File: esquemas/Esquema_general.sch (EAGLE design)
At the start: 36 parts

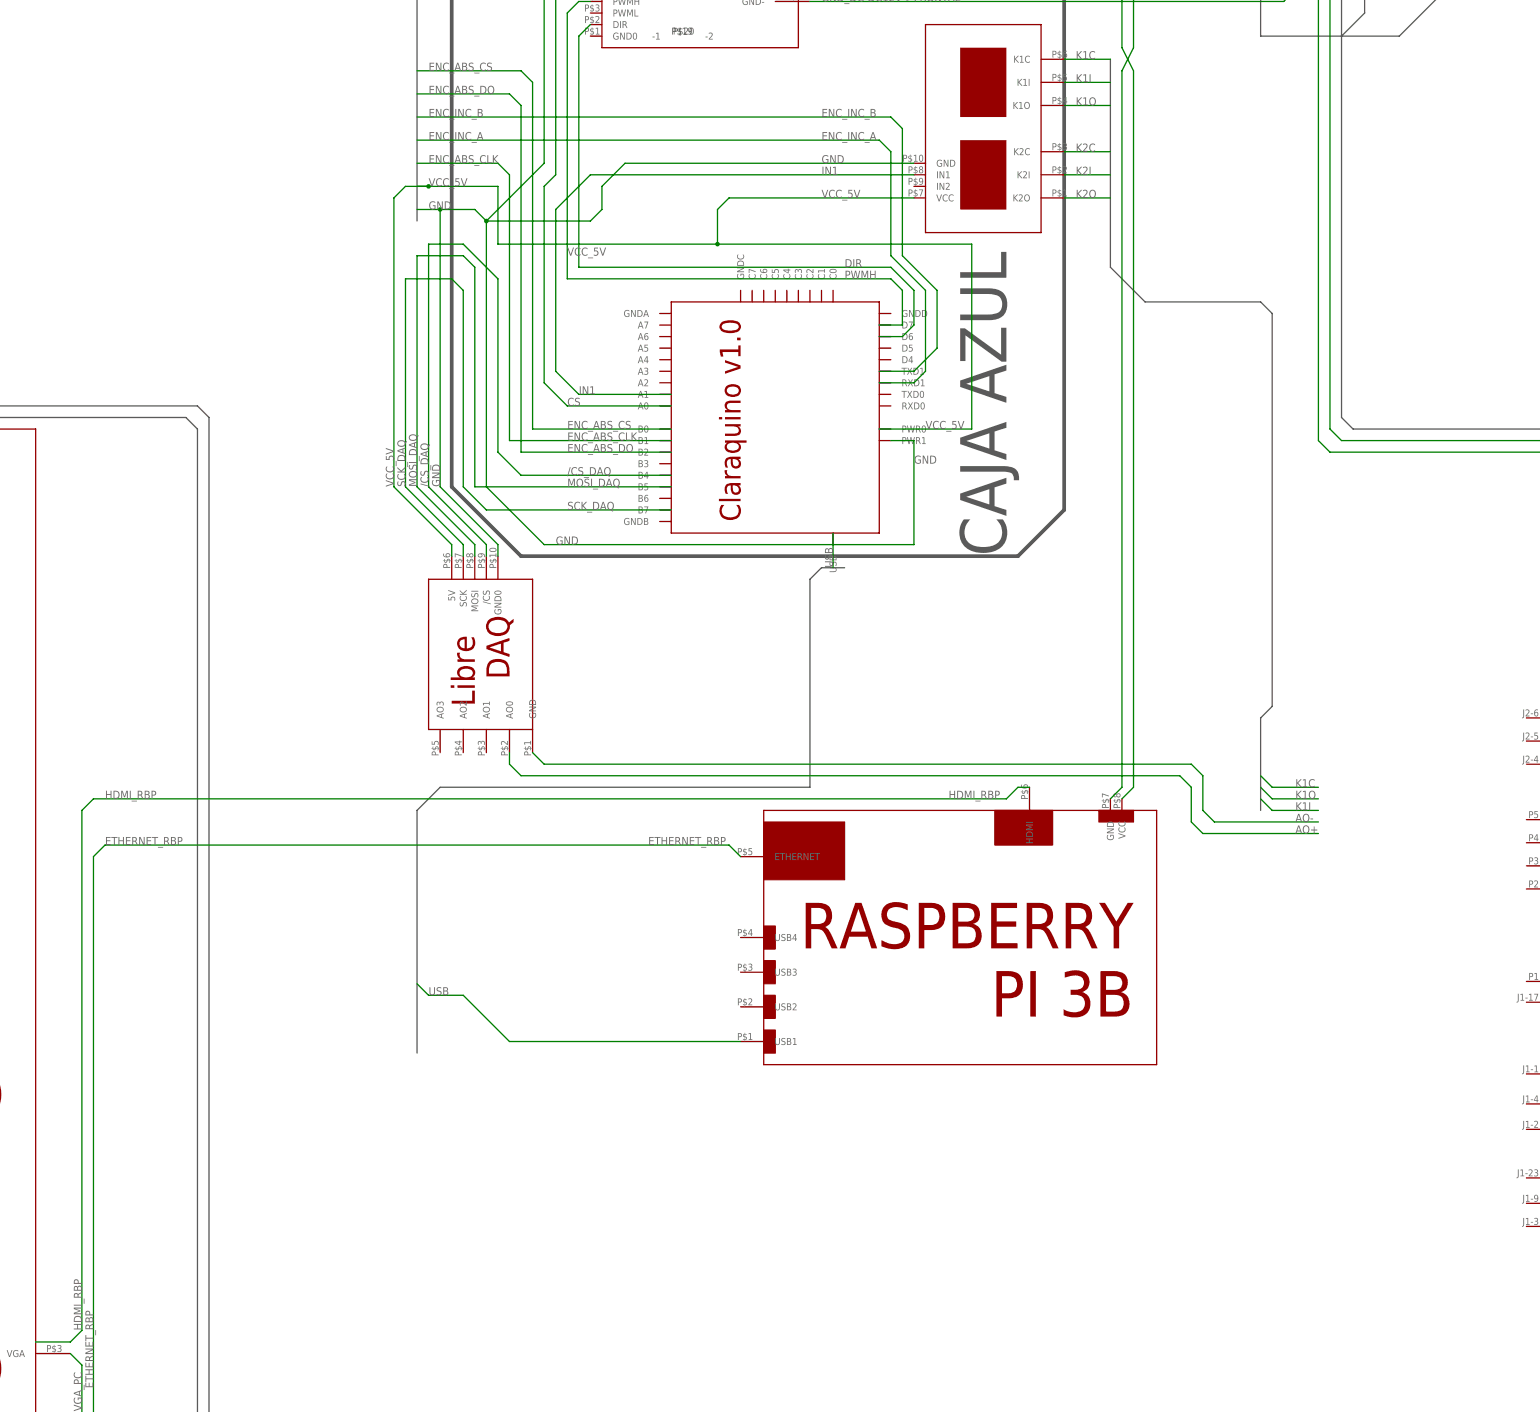
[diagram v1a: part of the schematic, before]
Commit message: sch eagle: quitar RBPI, añadir cables segundo rele
TODO: Curtis sch
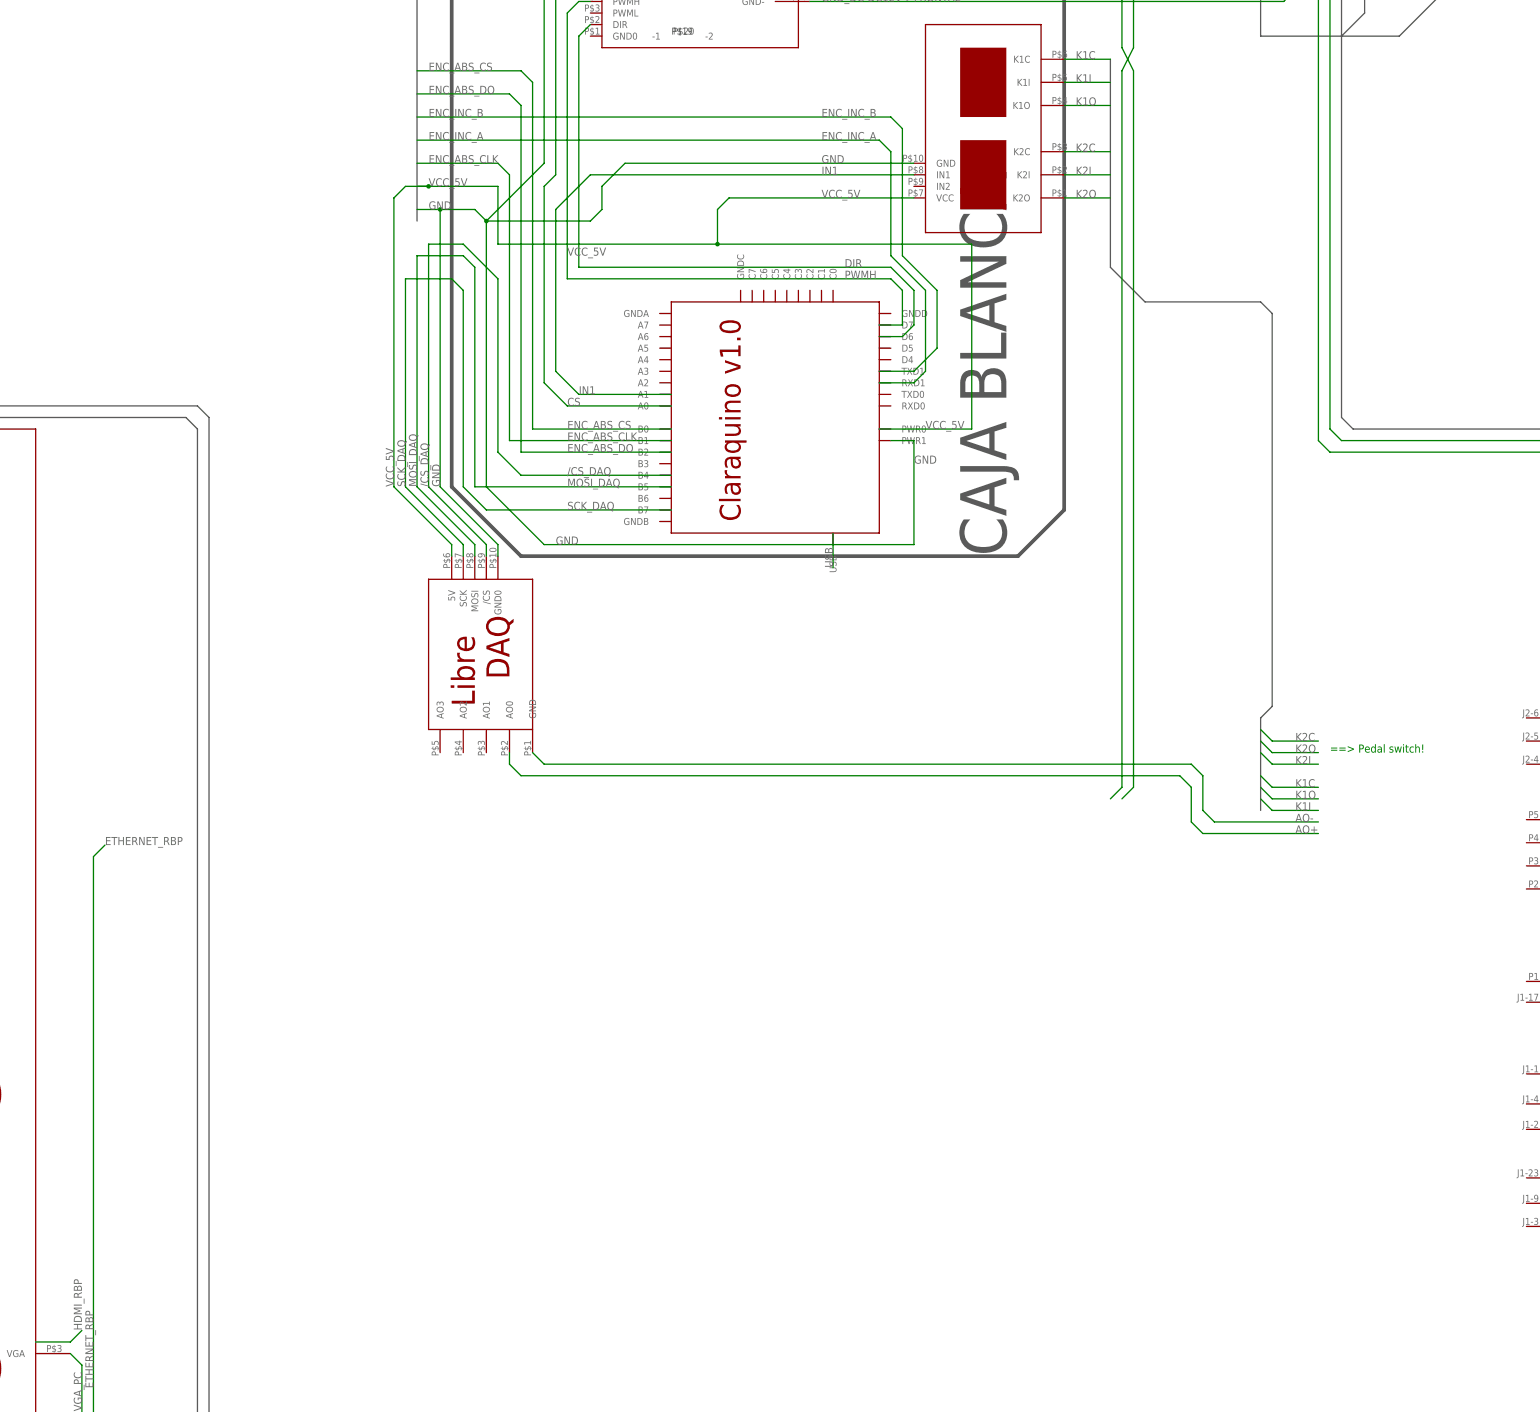
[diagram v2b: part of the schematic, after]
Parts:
- removed U$31: RASPBERRY_PI_3B, ecar:RASPBERRY_PI_3B
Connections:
- removed net ETHERNET_RBP: U$31.ETHERNET
- removed net HDMI_RBP: U$31.HDMI
- net 5V_GND: no longer U$31.GND
- net 5V_VCC: no longer U$31.VCC
- net USB: no longer U$31.USB1
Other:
- note added: "==> Pedal switch!"
- note removed: "CAJA AZUL"
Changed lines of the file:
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@@
 <?xml version="1.0" encoding="utf-8"?>
 <!DOCTYPE eagle SYSTEM "eagle.dtd">
-<eagle version="8.5.0">
+<eagle version="7.5.0">
 <drawing>
 <settings>
@@
 <part name="U$29" library="ecar" deviceset="SICK" device=""/>
 <part name="U$30" library="ecar" deviceset="MOTOR_SENSORES" device=""/>
-<part name="U$31" library="ecar" deviceset="RASPBERRY_PI_3B" device=""/>
 <part name="U$1" library="ecar" deviceset="MOTOR_DIRECCION" device=""/>
 <part name="U$34" library="ecar" deviceset="POLOLU_HIGH-POWER_MOTOR_DRIVER" device=""/>
 <part name="U$35" library="ecar" deviceset="AMPERIMETRO" device=""/>
 <part name="U$17" library="ecar" deviceset="GPS" device=""/>
-<part name="D1" library="display-hp" library_urn="urn:adsk.eagle:library:212" deviceset="HLMP6" device="" package3d_urn="urn:adsk.eagle:package:12992/1"/>
+<part name="D1" library="display-hp" deviceset="HLMP6" device=""/>
 <part name="U$32" library="ecar" deviceset="RELE_ARDUINO" device=""/>
 <part name="U$36" library="ecar" deviceset="LIBRE_DAQ" device=""/>
@@
 <wire x1="1356.36" y1="467.36" x2="1356.36" y2="193.04" width="0.508" layer="90"/>
 <wire x1="1356.36" y1="193.04" x2="1353.82" y2="190.5" width="0.508" layer="90"/>
-<wire x1="1353.82" y1="190.5" x2="1155.7" y2="190.5" width="0.508" layer="90"/>
 <wire x1="1155.7" y1="190.5" x2="1153.16" y2="193.04" width="0.508" layer="90"/>
 <wire x1="1153.16" y1="193.04" x2="1153.16" y2="467.36" width="0.508" layer="90"/>
@@
 <text x="1391.92" y="444.5" size="1.778" layer="97" rot="R90">Manguera_Encoder_Absoluto</text>
 <text x="1584.96" y="472.44" size="1.778" layer="97">Manguera_Encoder_Absoluto</text>
-<text x="1295.4" y="307.34" size="10.16" layer="97" rot="R90">CAJA AZUL</text>
+<text x="1295.4" y="307.34" size="10.16" layer="97" rot="R90">CAJA BLANCA</text>
 <text x="1348.74" y="269.24" size="17.78" layer="90" rot="R90">CAJA BLANCA</text>
+<text x="1366.52" y="264.16" size="1.778" layer="91">==&gt; Pedal switch!</text>
+<wire x1="1155.7" y1="190.5" x2="1353.82" y2="190.5" width="0.508" layer="90"/>
 </plain>
 <instances>
@@
 <instance part="U$29" gate="G$1" x="1770.38" y="342.9" rot="R270"/>
 <instance part="U$30" gate="G$1" x="1676.4" y="-45.72" rot="R90"/>
-<instance part="U$31" gate="G$1" x="1328.42" y="251.46" rot="R180"/>
 <instance part="U$1" gate="G$1" x="1617.98" y="490.22" rot="R90"/>
 <instance part="U$34" gate="G$1" x="1206.5" y="419.1"/>
@@
 <label x="1254.76" y="487.68" size="1.778" layer="95"/>
 <label x="1369.06" y="444.5" size="1.778" layer="95" rot="R90"/>
-</segment>
-</bus>
-<bus name="B$1">
-<segment>
-<wire x1="1165.86" y1="198.12" x2="1165.86" y2="251.46" width="0.762" layer="92"/>
-<wire x1="1165.86" y1="251.46" x2="1170.94" y2="256.54" width="0.762" layer="92"/>
-<wire x1="1170.94" y1="256.54" x2="1252.22" y2="256.54" width="0.762" layer="92"/>
-<wire x1="1252.22" y1="256.54" x2="1252.22" y2="302.26" width="0.762" layer="92"/>
-<wire x1="1252.22" y1="302.26" x2="1254.76" y2="304.8" width="0.762" layer="92"/>
-<wire x1="1254.76" y1="304.8" x2="1259.84" y2="304.8" width="0.762" layer="92"/>
 </segment>
 </bus>
@@
 <wire x1="1069.34" y1="474.98" x2="1323.34" y2="474.98" width="0.508" layer="91"/>
 <wire x1="1323.34" y1="474.98" x2="1323.34" y2="419.1" width="0.508" layer="91"/>
-<pinref part="U$31" gate="G$1" pin="GND"/>
 <wire x1="1318.26" y1="254" x2="1320.8" y2="256.54" width="0.508" layer="91"/>
 <wire x1="1320.8" y1="256.54" x2="1320.8" y2="414.02" width="0.508" layer="91"/>
@@
 <wire x1="1320.8" y1="419.1" x2="1323.34" y2="414.02" width="0.508" layer="91"/>
 <wire x1="1323.34" y1="414.02" x2="1323.34" y2="256.54" width="0.508" layer="91"/>
-<pinref part="U$31" gate="G$1" pin="VCC"/>
 <wire x1="1323.34" y1="256.54" x2="1320.8" y2="254" width="0.508" layer="91"/>
 <label x="1254.76" y="472.44" size="1.778" layer="95"/>
@@
 <label x="1310.64" y="386.08" size="1.778" layer="95"/>
 </segment>
+<segment>
+<wire x1="1351.28" y1="266.7" x2="1353.82" y2="264.16" width="0.508" layer="91"/>
+<wire x1="1353.82" y1="264.16" x2="1363.98" y2="264.16" width="0.508" layer="91"/>
+<label x="1358.9" y="264.16" size="1.778" layer="95"/>
+</segment>
 </net>
 <net name="K1C" class="0">
@@
 <label x="1310.64" y="396.24" size="1.778" layer="95"/>
 </segment>
+<segment>
+<wire x1="1351.28" y1="269.24" x2="1353.82" y2="266.7" width="0.508" layer="91"/>
+<wire x1="1353.82" y1="266.7" x2="1363.98" y2="266.7" width="0.508" layer="91"/>
+<label x="1358.9" y="266.7" size="1.778" layer="95"/>
+</segment>
 </net>
 <net name="K2I" class="0">
@@
 <label x="1310.64" y="391.16" size="1.778" layer="95"/>
 </segment>
+<segment>
+<wire x1="1351.28" y1="264.16" x2="1353.82" y2="261.62" width="0.508" layer="91"/>
+<wire x1="1353.82" y1="261.62" x2="1363.98" y2="261.62" width="0.508" layer="91"/>
+<label x="1358.9" y="261.62" size="1.778" layer="95"/>
+</segment>
 </net>
 <net name="HDMI_RBP" class="0">
 <segment>
-<pinref part="U$31" gate="G$1" pin="HDMI"/>
-<wire x1="1300.48" y1="256.54" x2="1297.94" y2="256.54" width="0.508" layer="91"/>
-<wire x1="1297.94" y1="256.54" x2="1295.4" y2="254" width="0.508" layer="91"/>
-<wire x1="1295.4" y1="254" x2="1094.74" y2="254" width="0.508" layer="91"/>
-<wire x1="1094.74" y1="254" x2="1092.2" y2="251.46" width="0.508" layer="91"/>
-<wire x1="1092.2" y1="251.46" x2="1092.2" y2="137.16" width="0.508" layer="91"/>
 <wire x1="1092.2" y1="137.16" x2="1089.66" y2="134.62" width="0.508" layer="91"/>
 <wire x1="1089.66" y1="134.62" x2="1082.04" y2="134.62" width="0.508" layer="91"/>
-<label x="1282.7" y="254" size="1.778" layer="95"/>
-<label x="1097.28" y="254" size="1.778" layer="95"/>
 <label x="1092.2" y="137.16" size="1.778" layer="95" rot="R90"/>
 </segment>
@@
 <net name="ETHERNET_RBP" class="0">
 <segment>
-<pinref part="U$31" gate="G$1" pin="ETHERNET"/>
-<wire x1="1236.98" y1="241.3" x2="1234.44" y2="243.84" width="0.508" layer="91"/>
-<wire x1="1234.44" y1="243.84" x2="1097.28" y2="243.84" width="0.508" layer="91"/>
 <wire x1="1097.28" y1="243.84" x2="1094.74" y2="241.3" width="0.508" layer="91"/>
 <wire x1="1094.74" y1="241.3" x2="1094.74" y2="-17.78" width="0.508" layer="91"/>
@@
 <wire x1="1013.46" y1="-60.96" x2="464.82" y2="-60.96" width="0.508" layer="91"/>
 <label x="1097.28" y="243.84" size="1.778" layer="95"/>
-<label x="1216.66" y="243.84" size="1.778" layer="95"/>
 <label x="1094.74" y="124.46" size="1.778" layer="95" rot="R90"/>
 <label x="1094.74" y="-15.24" size="1.778" layer="95" rot="R90"/>
@@
 <net name="USB" class="0">
 <segment>
-<wire x1="1176.02" y1="210.82" x2="1168.4" y2="210.82" width="0.508" layer="91"/>
-<wire x1="1168.4" y1="210.82" x2="1165.86" y2="213.36" width="0.508" layer="91"/>
-<label x="1168.4" y="210.82" size="1.778" layer="95"/>
-<pinref part="U$31" gate="G$1" pin="USB1"/>
-<wire x1="1176.02" y1="210.82" x2="1186.18" y2="200.66" width="0.508" layer="91"/>
-<wire x1="1186.18" y1="200.66" x2="1236.98" y2="200.66" width="0.508" layer="91"/>
-</segment>
-<segment>
 <pinref part="U$24" gate="G$1" pin="USB"/>
 <wire x1="1257.3" y1="312.42" x2="1257.3" y2="304.8" width="0.1524" layer="91"/>
@@
 which will not be processed correctly with this version.
 </note>
-<note version="8.2" severity="warning">
-Since Version 8.2, EAGLE supports online libraries. The ids
-of those online libraries will not be understood (or retained)
-with this version.
-</note>
-<note version="8.3" severity="warning">
-Since Version 8.3, EAGLE supports URNs for individual library
-assets (packages, symbols, and devices). The URNs of those assets
-will not be understood (or retained) with this version.
-</note>
-<note version="8.3" severity="warning">
-Since Version 8.3, EAGLE supports the association of 3D packages
-with devices in libraries, schematics, and board files. Those 3D
-packages will not be understood (or retained) with this version.
-</note>
 </compatibility>

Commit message: Update Esquema_general.sch
Primera actualización de componentes.
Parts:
- removed U$25: PHIDGETS_ENCODER, ecar:PHIDGETS_ENCODER
- removed U$4, U$5, U$6: VOLTIMETRO, ecar:VOLTIMETRO
- added U$31, U$37: MOTOR_DIRECCION, ecar:MOTOR_DIRECCION
- added U$33: POLOLU_HIGH-POWER_MOTOR_DRIVER, ecar:POLOLU_HIGH-POWER_MOTOR_DRIVER
- U$1: value MOTOR_DIRECCION -> CLARAQUINO_V1.0; device ecar:MOTOR_DIRECCION -> ecar:CLARAQUINO_V1.0
- U$2: value DAQ_NI -> FUENTE_24V; device ecar:DAQ_NI -> ecar:FUENTE_24V
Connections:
- removed net AMARILLO_A2_M-: U$6.V-
- removed net AMARILLO_AO+: U$2.AI6
- removed net AMARILLO_U_VOLT3: U$2.AI7, U$6.VOUT
- removed net AZUL_U_VOLT1: U$2.AI0, U$4.VOUT
- removed net BLANCO_F2: U$5.V+
- removed net MARRON_GND_VOLT2: U$2.AI10, U$5.VOUT_GND
- removed net NARANJA_GND_U1: U$2.AI8, U$4.VOUT_GND
- removed net NARANJA_VOUT_A2: U$2.AI13
- removed net NEGRO_F1: U$5.V-
- removed net ROJO_GND_VOLT3: U$2.AI15, U$6.VOUT_GND
- removed net USB_PHIDGET_ENCODER_PC: U$16.USB1, U$25.USB
- removed net VERDE_A1_M+: U$6.V+
- removed net VERDE_U_VOLT2: U$2.AI2, U$5.VOUT
- removed net VERDE_VOUT_A1-M+: U$2.AI5
- net AMARILLO_OUTPUT_HONEYWELL: no longer U$2.AI3
- net BAT_1: no longer U$4.V-
- net BAT_8+: no longer U$4.V+
- net ENC_INC_A: now also U$37.6.A; no longer U$1.6.A
- net ENC_INC_B: now also U$37.B; no longer U$1.B
- net ENC_L_5V: no longer U$25.E0_5V
- net ENC_L_GND: no longer U$25.E0_GND
- net ENC_L_OUT_A: no longer U$25.E0_A
- net ENC_L_OUT_B: no longer U$25.E0_B
- net ENC_L_OUT_Z: no longer U$25.E0_INDEX
- net ENC_R_5V: no longer U$25.E1_5V
- net ENC_R_GND: no longer U$25.E1_GND
- net ENC_R_OUT_A: no longer U$25.E1_A
- net ENC_R_OUT_B: no longer U$25.E1_B
- net ENC_R_OUT_Z: no longer U$25.E1_INDEX
- net GND: now also U$37.3.GND; no longer U$1.3.GND
- net GND_DC-DC24V->SENSORES: no longer U$4.GND, U$5.GND, U$6.GND
- net MARRON_VCC_HONEYWELL: no longer U$2.+5V
- net MOTOR_DIRECCION_+: now also U$37.MOTOR+; no longer U$1.MOTOR+
- net MOTOR_DIRECCION_-: now also U$37.MOTOR-; no longer U$1.MOTOR-
- net N.C.: now also U$37.1.NC, U$37.10.I, U$37.4.NC, U$37.5./A, U$37.7./B, U$37.9/I; no longer U$1.1.NC, U$1.10.I, U$1.4.NC, U$1.5./A, U$1.7./B, U$1.9/I
- net NEGRO_-VCC_HONEYWELL: no longer U$2.AI11, U$2.DGND1
- net ROJO_VOUT_LEM: no longer U$2.AI1
- net VCC_5V: now also U$37.2.VCC; no longer U$1.2.VCC
- net VCC_DC-DC24V->SENSORES: no longer U$4.VCC, U$5.VCC, U$6.VCC
- net VERDE_GND_LEM: no longer U$2.AI9
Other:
- note removed: "AZUL_VACIO(M2) MARRON_VACIO(M2)"
